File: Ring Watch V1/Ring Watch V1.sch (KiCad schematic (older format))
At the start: 5 parts

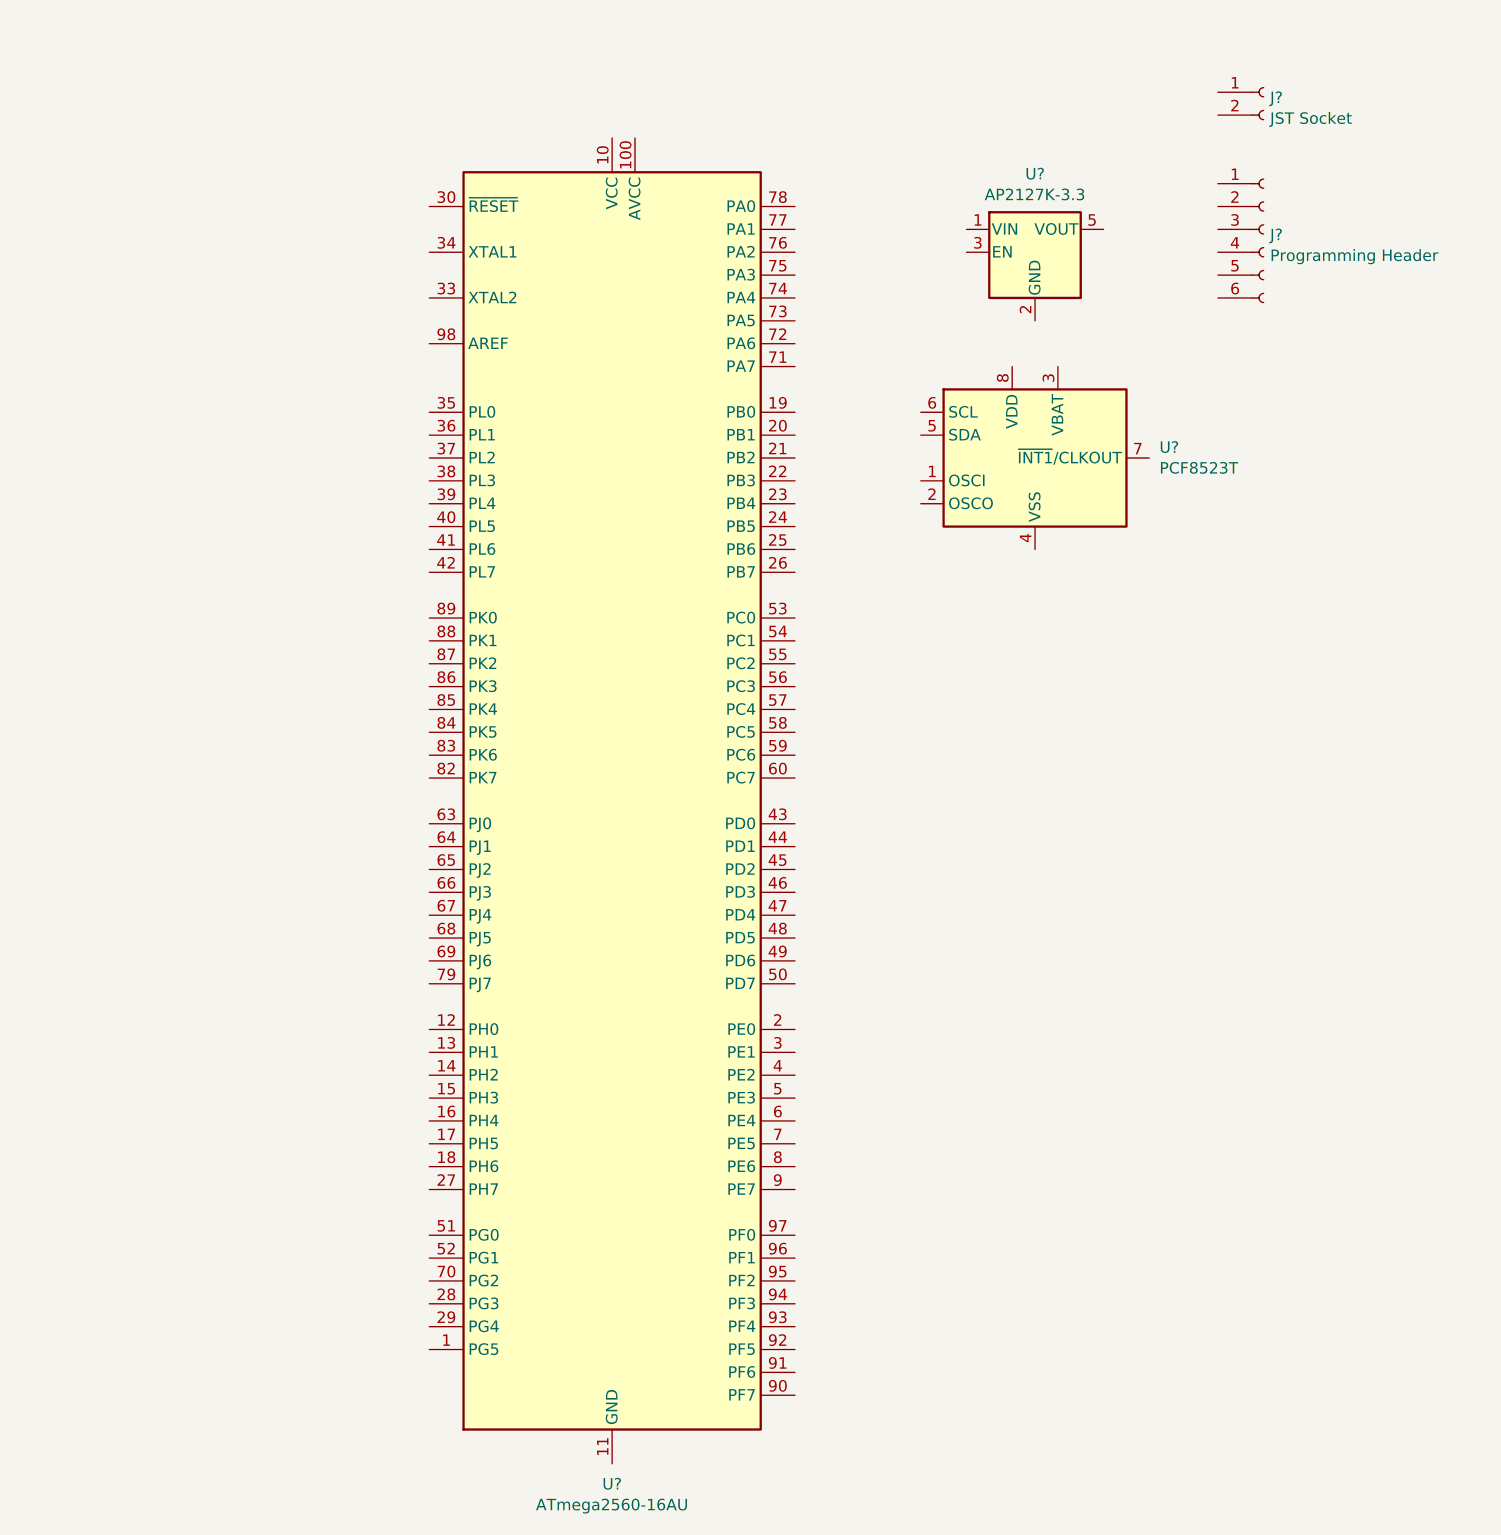
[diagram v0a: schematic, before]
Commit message: changed to ATtiny85, maybe use RGB first
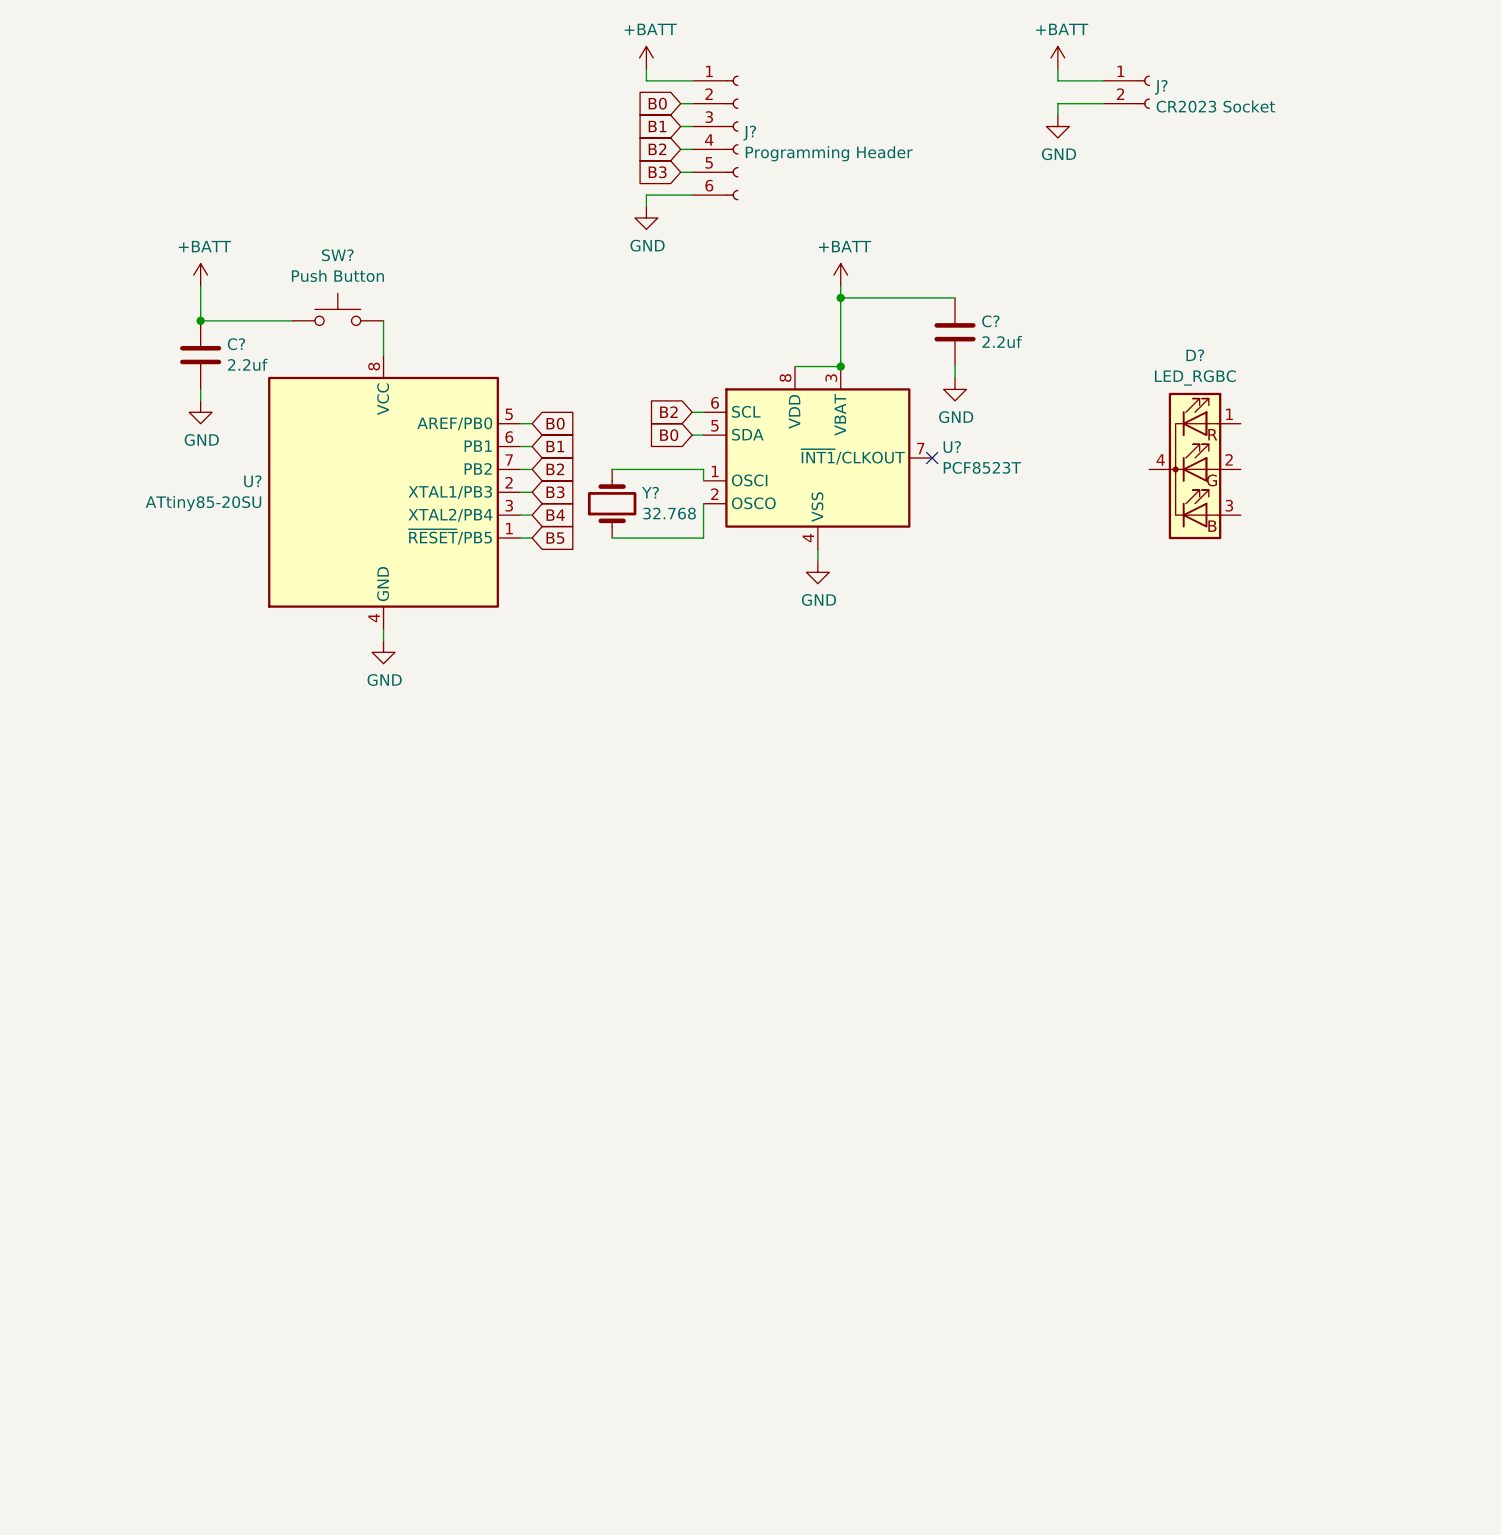
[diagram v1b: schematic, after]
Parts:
- removed U?: ATmega2560-16AU, Package_QFP:TQFP-100_14x14mm_P0.5mm, symbol MCU_Microchip_ATmega:ATmega2560-16AU
- removed U?: AP2127K-3.3, Package_TO_SOT_SMD:SOT-23-5, symbol Regulator_Linear:AP2127K-3.3
- added C? (x2): 2.2uf, symbol Device:C
- added D?: LED_RGBC, symbol Device:LED_RGBC
- added SW?: Push Button, symbol Switch:SW_Push
- added U?: ATtiny85-20SU, Package_SO:SOIJ-8_5.3x5.3mm_P1.27mm, symbol MCU_Microchip_ATtiny:ATtiny85-20SU
- added Y?: 32.768, symbol Device:Crystal
- J?: value JST Socket -> CR2023 Socket
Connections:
- net +BATT: now reaches J?.1 (Pin_1)
- net +BATT: now also J?.1 (Pin_1), U?.3 (VBAT), U?.8 (VDD), C?.1, C?.1, SW?.1
- net B0: now reaches J?.2 (Pin_2)
- net B0: now also U?.5 (SDA), U?.5 (AREF/PB0)
- net B1: now reaches J?.3 (Pin_3)
- net B1: now also U?.6 (PB1)
- net B2: now reaches J?.4 (Pin_4)
- net B2: now also U?.6 (SCL), U?.7 (PB2)
- net B3: now reaches J?.5 (Pin_5)
- net B3: now also U?.2 (XTAL1/PB3)
- net GND: now reaches J?.6 (Pin_6)
- net GND: now also J?.2 (Pin_2), U?.4 (VSS), C?.2, C?.2, U?.4 (GND)
- net at U?.1 (OSCI): now also Y?.2
- net at U?.2 (OSCO): now also Y?.1
- new net: SW?.2, U?.8 (VCC)
- new net B4: U?.3 (XTAL2/PB4)
- new net B5: U?.1 (~RESET~/PB5)
- no-connect marks 0 -> 1
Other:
- moved on the sheet: J?, U?

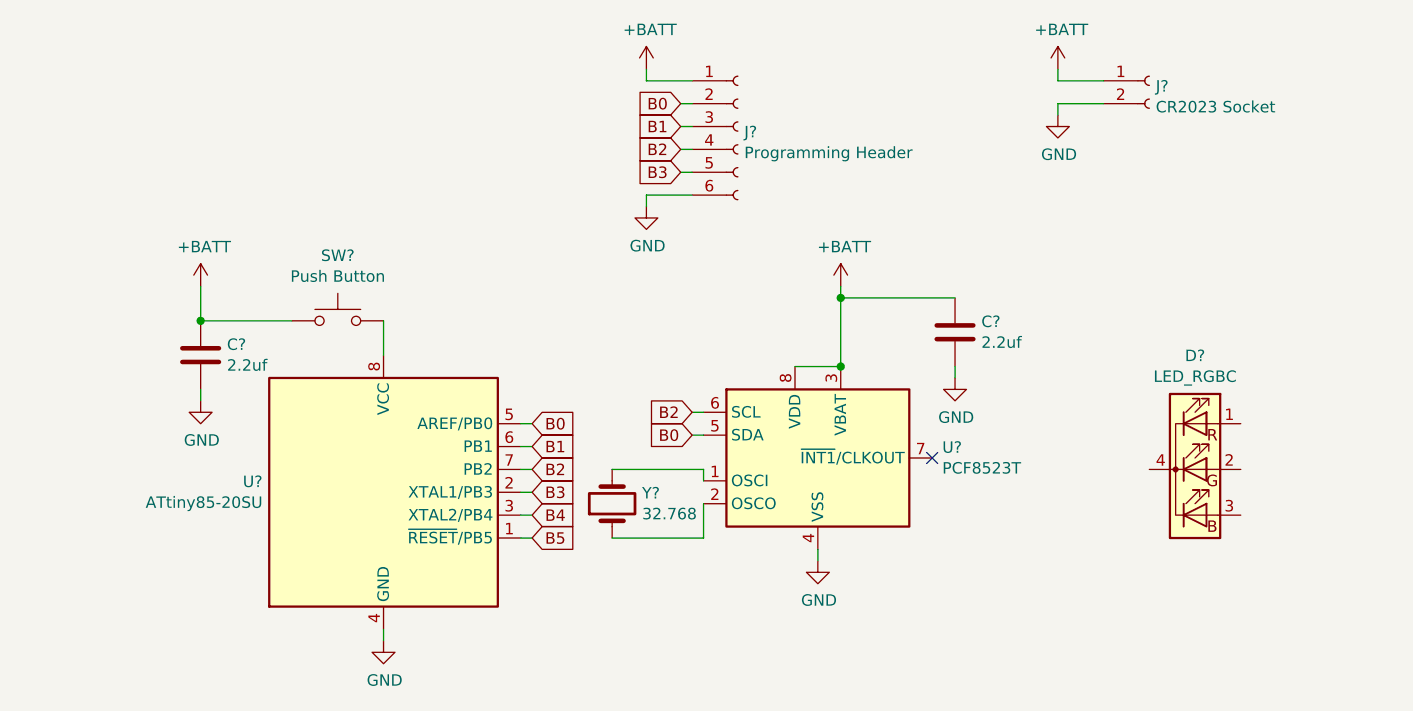
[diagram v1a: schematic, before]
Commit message: new mechanical switch design for input power to micro
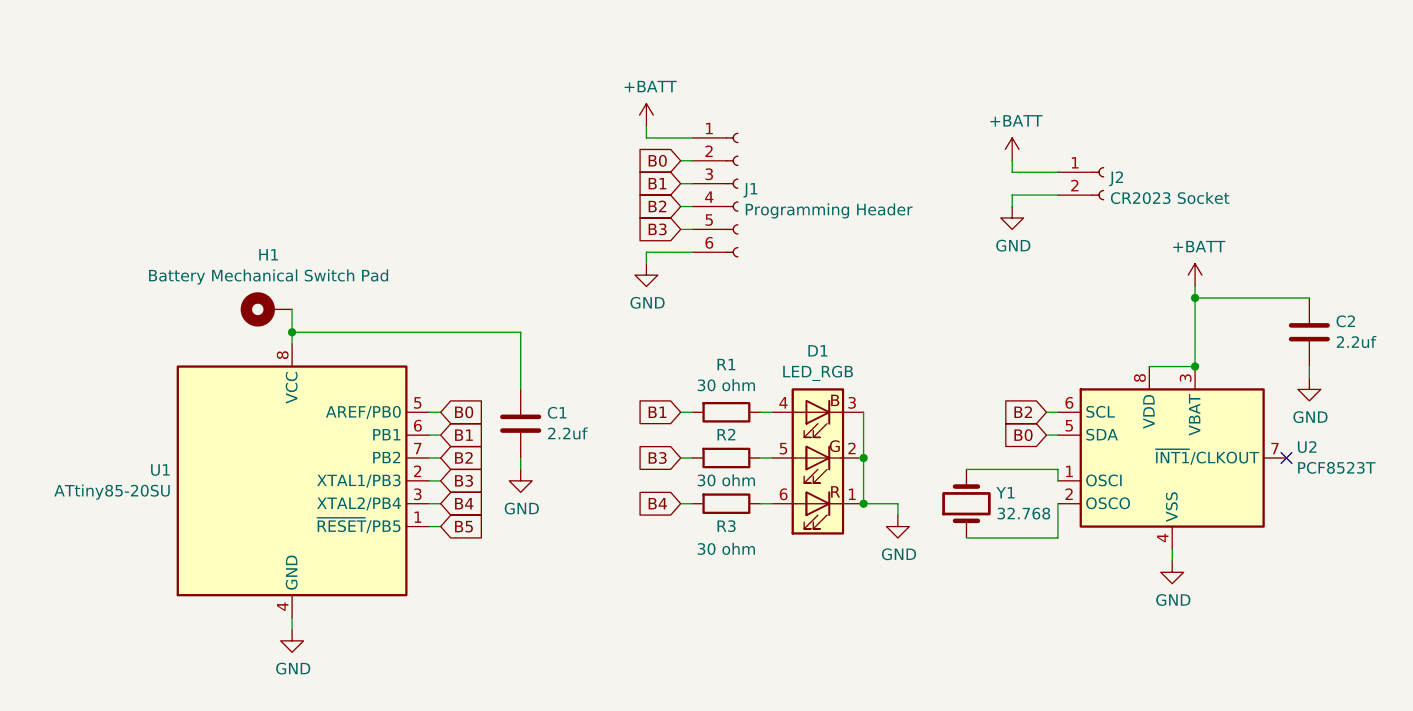
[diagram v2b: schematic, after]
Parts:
- removed D?: LED_RGBC, symbol Device:LED_RGBC
- removed SW?: Push Button, symbol Switch:SW_Push
- added D1: LED_RGB, LED_SMD:LED_RGB_5050-6, symbol Device:LED_RGB
- added H1: Battery Mechanical Switch Pad, TestPoint:TestPoint_Pad_4.0x4.0mm, symbol Mechanical:MountingHole_Pad
- added R1, R2, R3: 30 ohm, Resistor_SMD:R_0805_2012Metric_Pad1.15x1.40mm_HandSolder, symbol Device:R
- C1, C2: renamed from C?; footprint (none) -> Capacitor_SMD:C_0805_2012Metric_Pad1.15x1.40mm_HandSolder
- J1: renamed from J?; footprint (none) -> Connector_PinHeader_2.54mm:PinHeader_2x03_P2.54mm_Vertical
- J2: renamed from J?; footprint (none) -> Battery:BatteryHolder_Keystone_3034_1x20mm
- Y1: renamed from Y?; footprint (none) -> Crystal:Crystal_SMD_Abracon_ABM7-2Pin_6.0x3.5mm
- gave numbers to parts that had none: 2
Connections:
- net +BATT: no longer C1.1
- net B1: now also R1.2
- net B3: now also R2.2
- net B4: now also R3.2
- net GND: now also D1.1 (RK), D1.2 (GK), D1.3 (BK)
- net at U1.8 (VCC): now also C1.1, H1.1
- new net: D1.4 (BA), R1.1
- new net: D1.5 (GA), R2.1
- new net: D1.6 (RA), R3.1
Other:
- moved on the sheet: C1, C2, J1, J2, U1, U2, Y1

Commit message: almost done placing components
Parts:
- J1: footprint Connector_PinHeader_2.54mm:PinHeader_2x03_P2.54mm_Vertical -> Connector_PinHeader_1.00mm:PinHeader_2x03_P1.00mm_Vertical
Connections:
- net +BATT: no longer U2.8 (VDD)
- net B3: no longer J1.5 (Pin_5)
- net B5: now also J1.5 (Pin_5)
- net at C1.1, H1.1, U1.8 (VCC): now also U2.8 (VDD)
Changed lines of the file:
@@
 F 0 "J1" H 4078 1576 50  0000 L CNN
 F 1 "Programming Header" H 4078 1485 50  0000 L CNN
-F 2 "Connector_PinHeader_2.54mm:PinHeader_2x03_P2.54mm_Vertical" H 4050 1600 50  0001 C CNN
+F 2 "Connector_PinHeader_1.00mm:PinHeader_2x03_P1.00mm_Vertical" H 4050 1600 50  0001 C CNN
 F 3 "~" H 4050 1600 50  0001 C CNN
 	1    4050 1600
@@
 	1    0    0    -1
 $EndComp
-Wire Wire Line
-	5850 2400 6050 2400
-Connection ~ 6050 2400
 $Comp
 L Device:C C2
@@
 B2
 Text GLabel 3800 1800 0    50   Input ~ 0
-B3
+B5
 Wire Wire Line
 	3800 1500 3850 1500
@@
 	0    -1   -1   0
 $EndComp
+Wire Wire Line
+	3100 2250 5850 2250
+Wire Wire Line
+	5850 2250 5850 2400
+Connection ~ 3100 2250
 $EndSCHEMATC

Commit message: more routing, board shape near final
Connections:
- net +BATT: no longer J1.1 (Pin_1)
- net at C1.1, H1.1, U1.8 (VCC)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: now also J1.1 (Pin_1)
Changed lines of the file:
@@
 B2
-$Comp
-L power:+BATT #PWR0108
-U 1 1 5FBE4D9A
-P 3650 1350
-F 0 "#PWR0108" H 3650 1200 50  0001 C CNN
-F 1 "+BATT" H 3665 1523 50  0000 C CNN
-F 2 "" H 3650 1350 50  0001 C CNN
-F 3 "" H 3650 1350 50  0001 C CNN
-	1    3650 1350
-	1    0    0    -1
-$EndComp
-Wire Wire Line
-	3850 1400 3650 1400
 $Comp
 L power:GND #PWR0109
@@
 Wire Wire Line
 	5250 1500 5250 1550
-Wire Wire Line
-	3650 1350 3650 1400
 $Comp
 L Device:LED_RGB D1
@@
 	5850 2250 5850 2400
 Connection ~ 3100 2250
+Wire Wire Line
+	3100 1400 3100 2250
+Wire Wire Line
+	3100 1400 3850 1400
 $EndSCHEMATC

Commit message: more layout changes
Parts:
- H1: footprint TestPoint:TestPoint_Pad_4.0x4.0mm -> TestPoint:TestPoint_Keystone_5019_Minature
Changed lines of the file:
@@
 F 0 "H1" V 2237 2153 50  0000 C CNN
 F 1 "Battery Mechanical Switch Pad" V 2146 2153 50  0000 C CNN
-F 2 "TestPoint:TestPoint_Pad_4.0x4.0mm" H 2000 2150 50  0001 C CNN
+F 2 "TestPoint:TestPoint_Keystone_5019_Minature" H 2000 2150 50  0001 C CNN
 F 3 "~" H 2000 2150 50  0001 C CNN
 	1    2000 2150

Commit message: minor changes, need to place GND polygons
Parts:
- added C3: 2.2uf, Capacitor_SMD:C_0805_2012Metric_Pad1.15x1.40mm_HandSolder, symbol Device:C
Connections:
- net GND: now also C3.2
- net at C1.1, H1.1, J1.1 (Pin_1)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: now also C3.1
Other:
- moved on the sheet: C2, D1, J1, J2, R1, R2, R3, U2, Y1
